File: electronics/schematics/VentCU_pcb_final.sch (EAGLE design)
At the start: 12 parts, among them U1 ADS1115IDGST, X1 TERMINAL-BLOCK-3.5MM-6-PIN-RO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, X2 TERMINAL-BLOCK-3.5MM-4-PIN-RO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

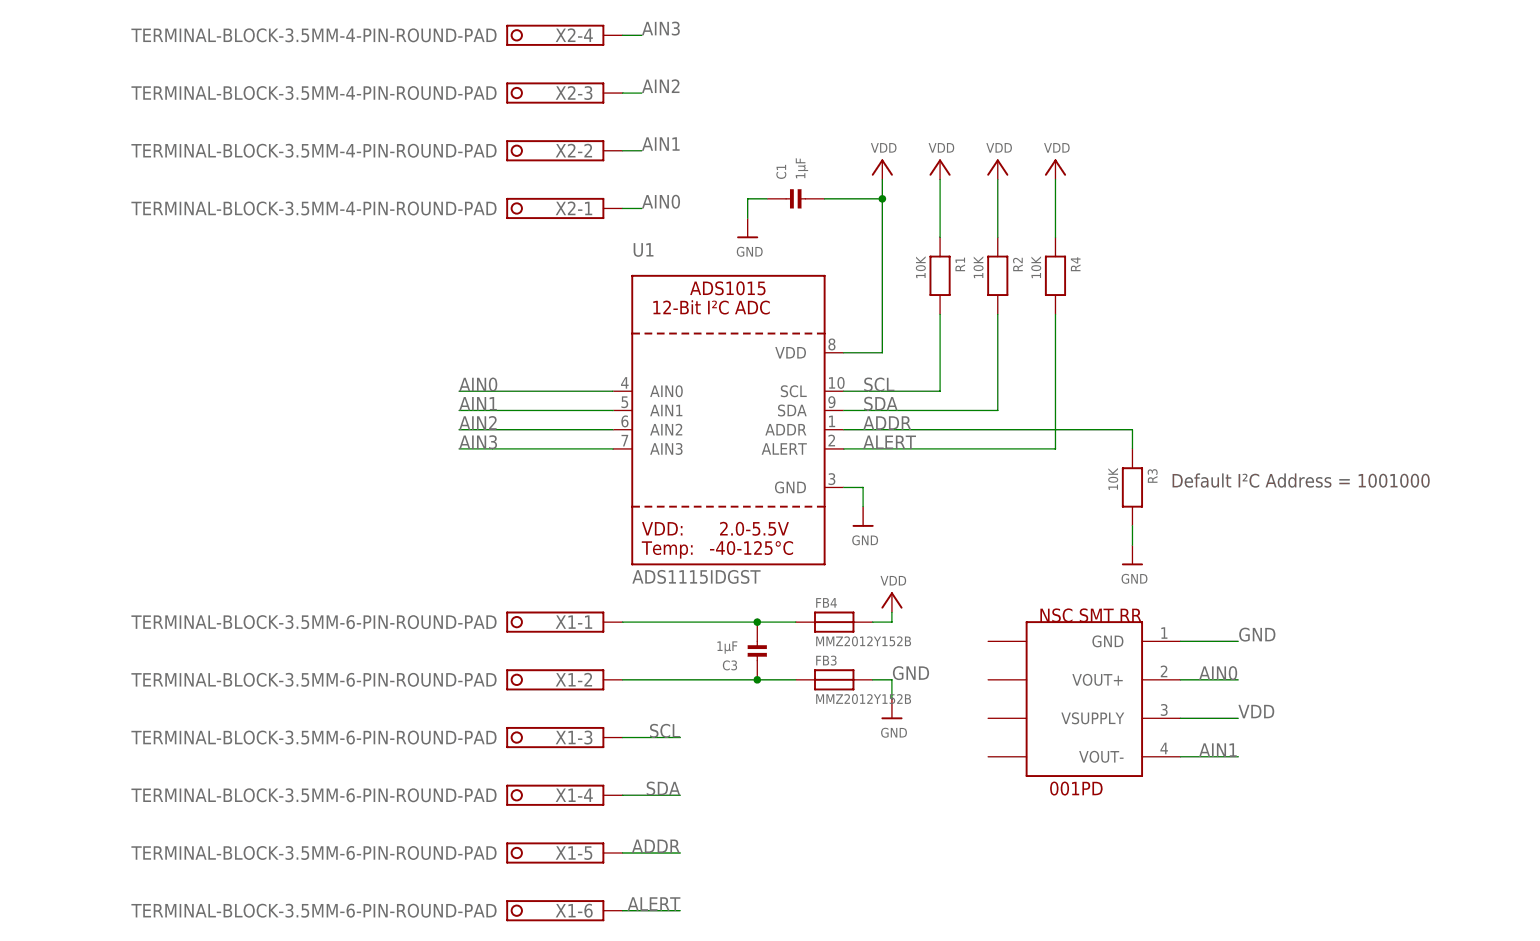
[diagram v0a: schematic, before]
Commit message: Updated design for better signal integrity, size
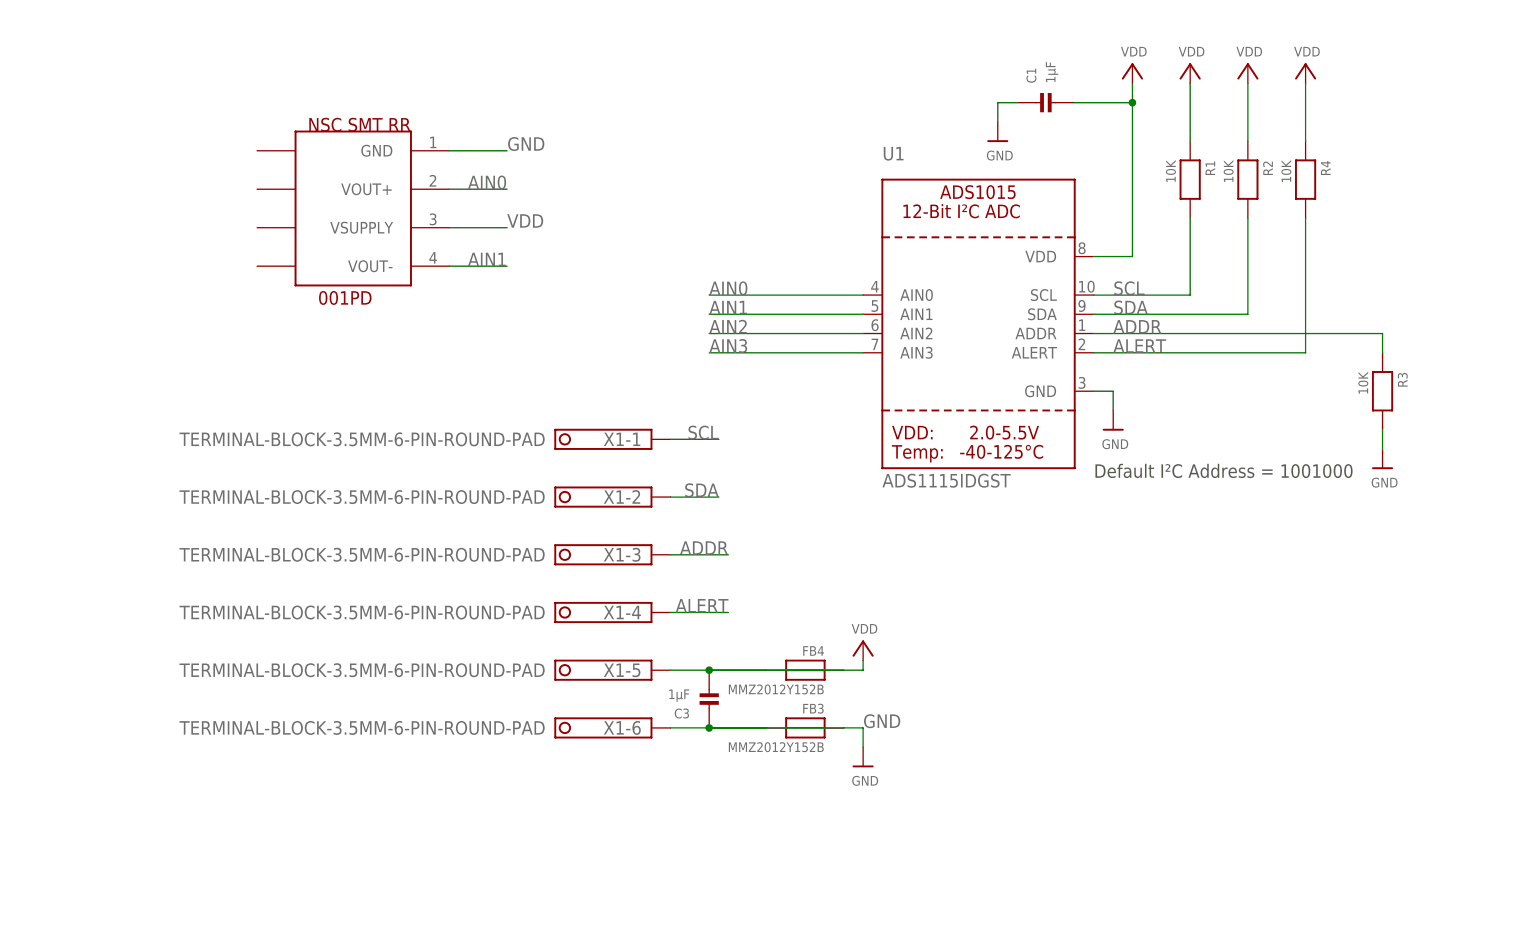
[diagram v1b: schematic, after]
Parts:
- removed X2: TERMINAL-BLOCK-3.5MM-4-PIN-ROUND-PAD, Rembrandt Electronics - Terminal Block 3-5mm v1-0:TERMINAL-BLOCK-3.5MM-4-PIN-ROUND-PAD
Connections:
- net ADDR: now also X1-3.K; no longer X1-5.K
- net AIN0: no longer X2-1.K
- net AIN1: no longer X2-2.K
- net AIN2: no longer X2-3.K
- net AIN3: no longer X2-4.K
- net ALERT: now also X1-4.K; no longer X1-6.K
- net GND: now also C3.P$1, FB3.P$1; no longer FB3.P$2
- net N$1: now also FB4.P$2, X1-5.K; no longer C3.P$2, FB4.P$1, X1-1.K
- net N$2: now also FB3.P$2, X1-6.K; no longer C3.P$1, FB3.P$1, X1-2.K
- net SCL: now also X1-1.K; no longer X1-3.K
- net SDA: now also X1-2.K; no longer X1-4.K
- net VDD: now also C3.P$2, FB4.P$1; no longer FB4.P$2
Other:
- moved on the sheet: C1, C3, FB3, FB4, R1, R2, R3, R4, U1, X1-1, X1-2, X1-3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
